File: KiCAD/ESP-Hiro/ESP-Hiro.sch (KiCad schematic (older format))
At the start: 17 parts, among them U1 TPS54331D

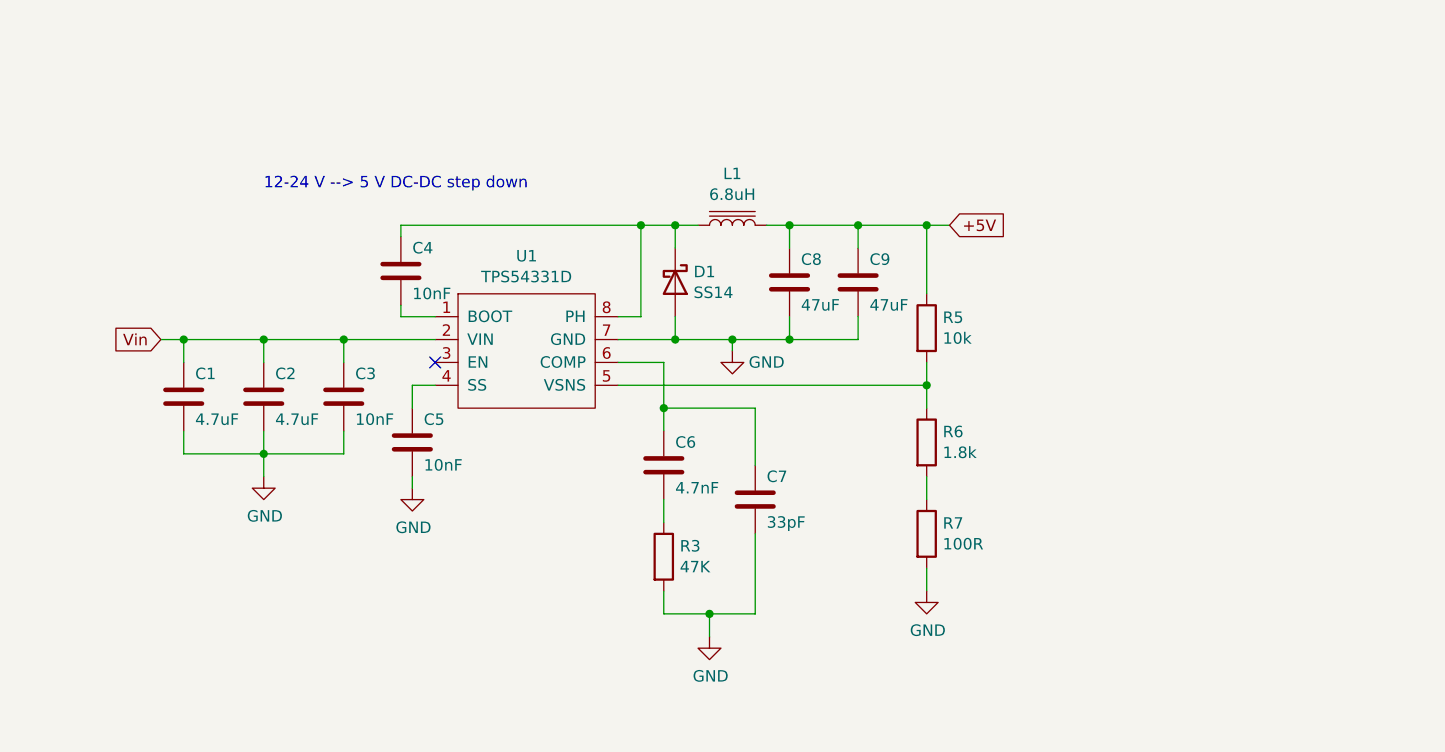
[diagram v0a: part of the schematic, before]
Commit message: Add 3.3 V LDO to schematic
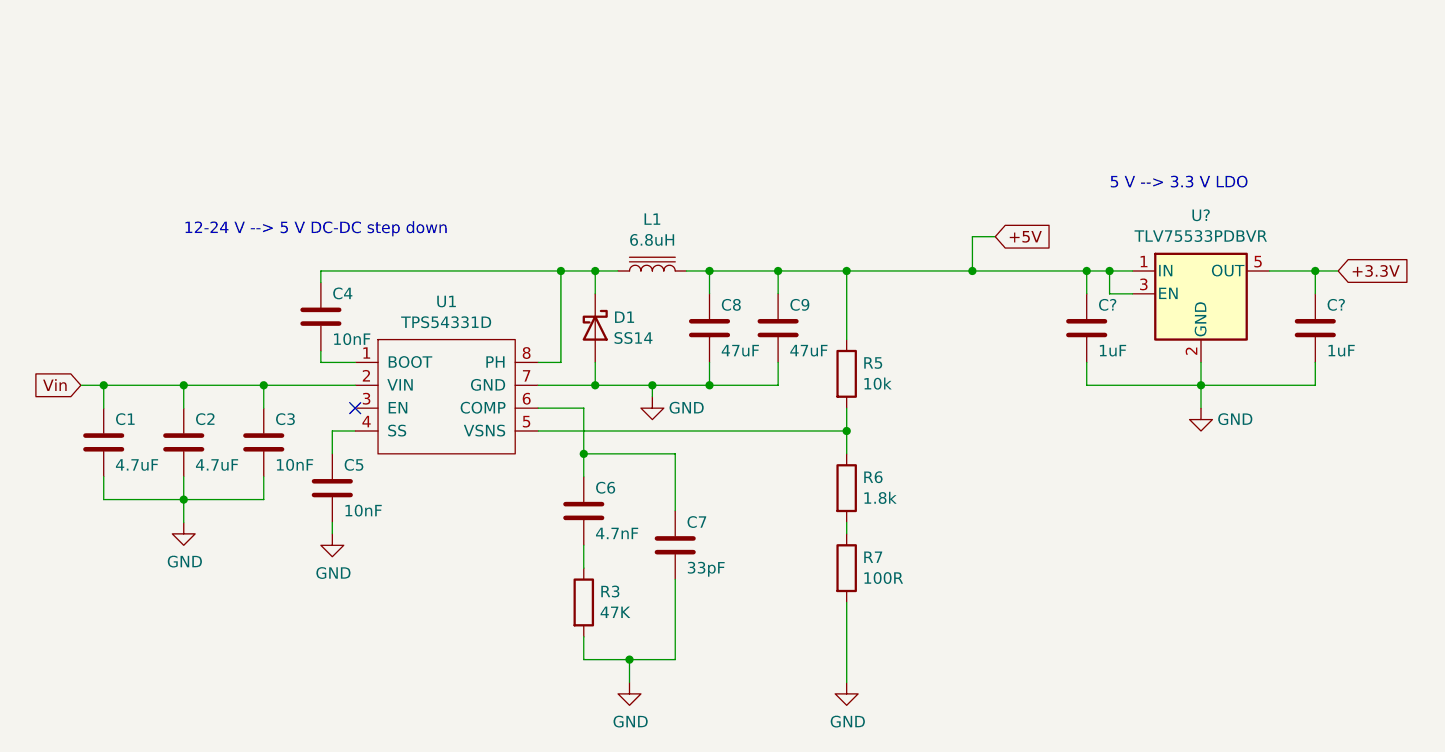
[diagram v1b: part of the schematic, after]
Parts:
- added C? (x2): 1uF, Capacitor_SMD:C_0603_1608Metric, symbol Device:C
- added U?: TLV75533PDBVR, Package_TO_SOT_SMD:SOT-23-5, symbol Regulator_Linear:TLV75533PDBV
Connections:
- net +5V: now also C?.1, U?.1 (IN), U?.3 (EN)
- net GND: now also C?.2, C?.2, U?.2 (GND)
- new net +3.3V: C?.1, U?.5 (OUT)
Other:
- note added: "5 V --> 3.3 V LDO"
- moved on the sheet: C1, C2, C3, C4, C5, C6, C7, C8, C9, D1, L1, R3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

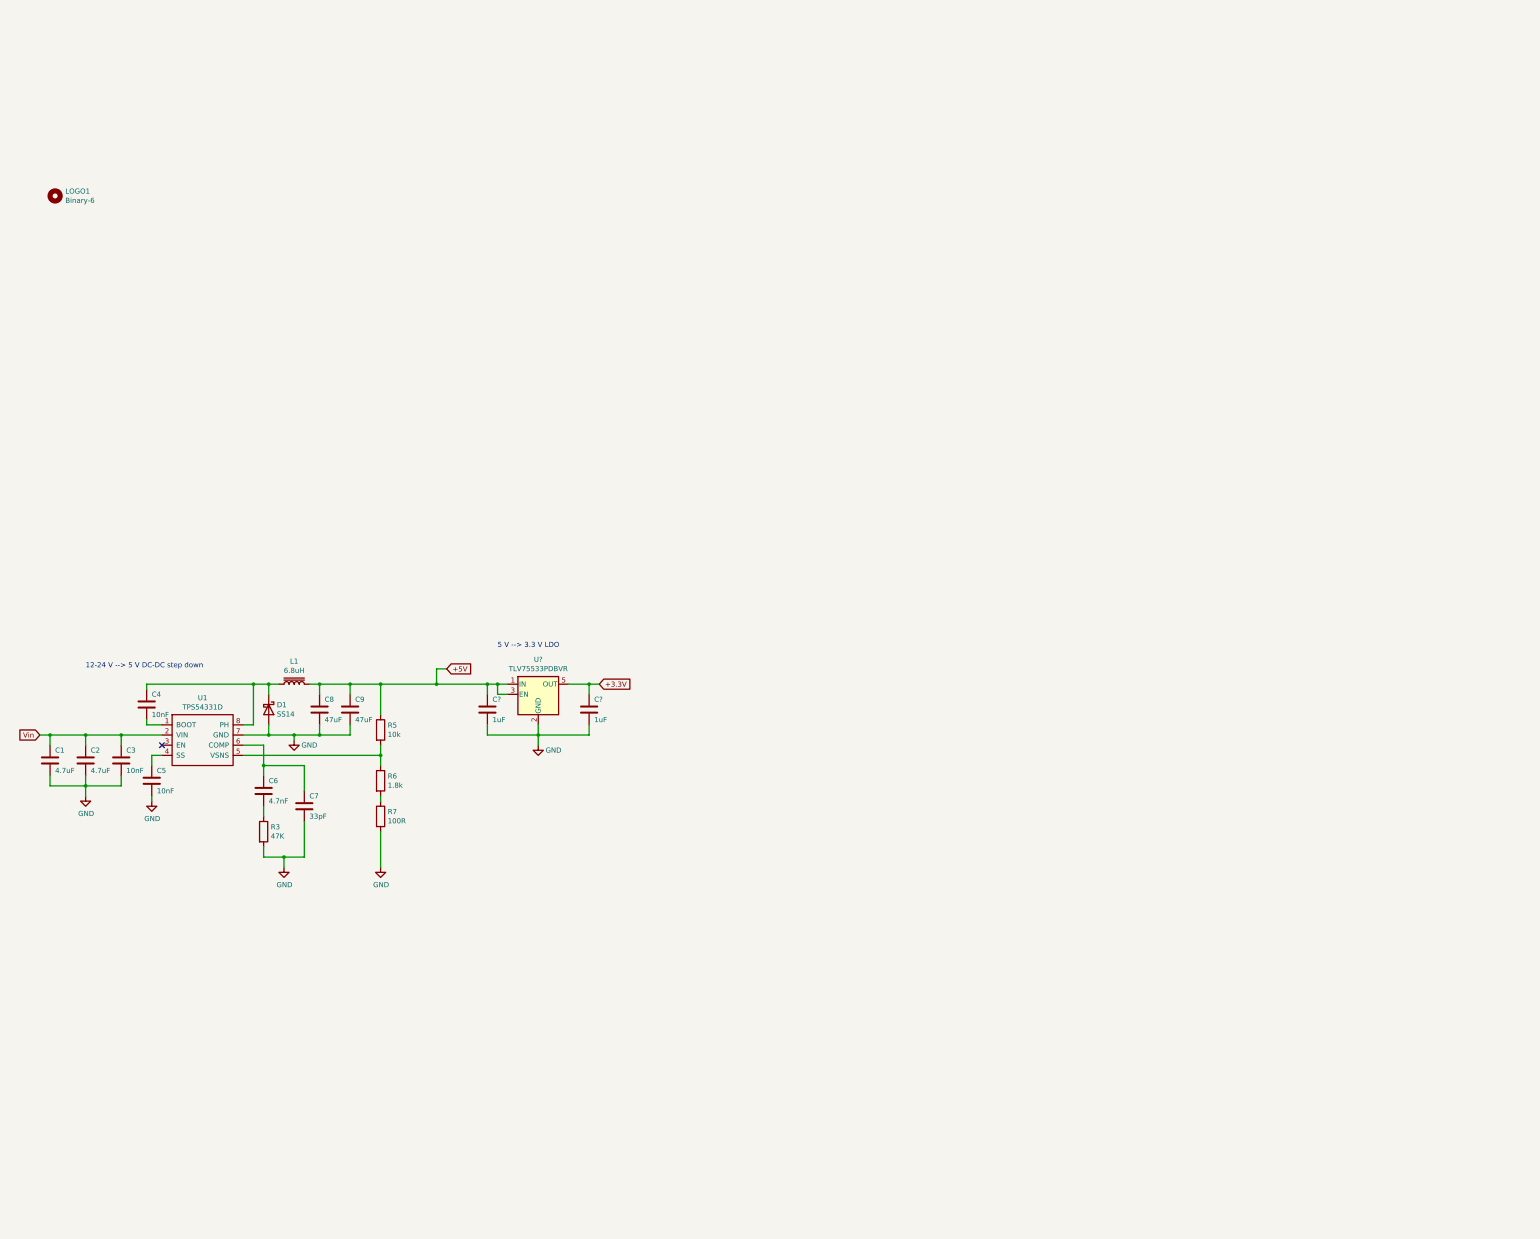
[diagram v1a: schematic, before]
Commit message: Paste more reusable blocks from old ESP-Hiro version into new schematic
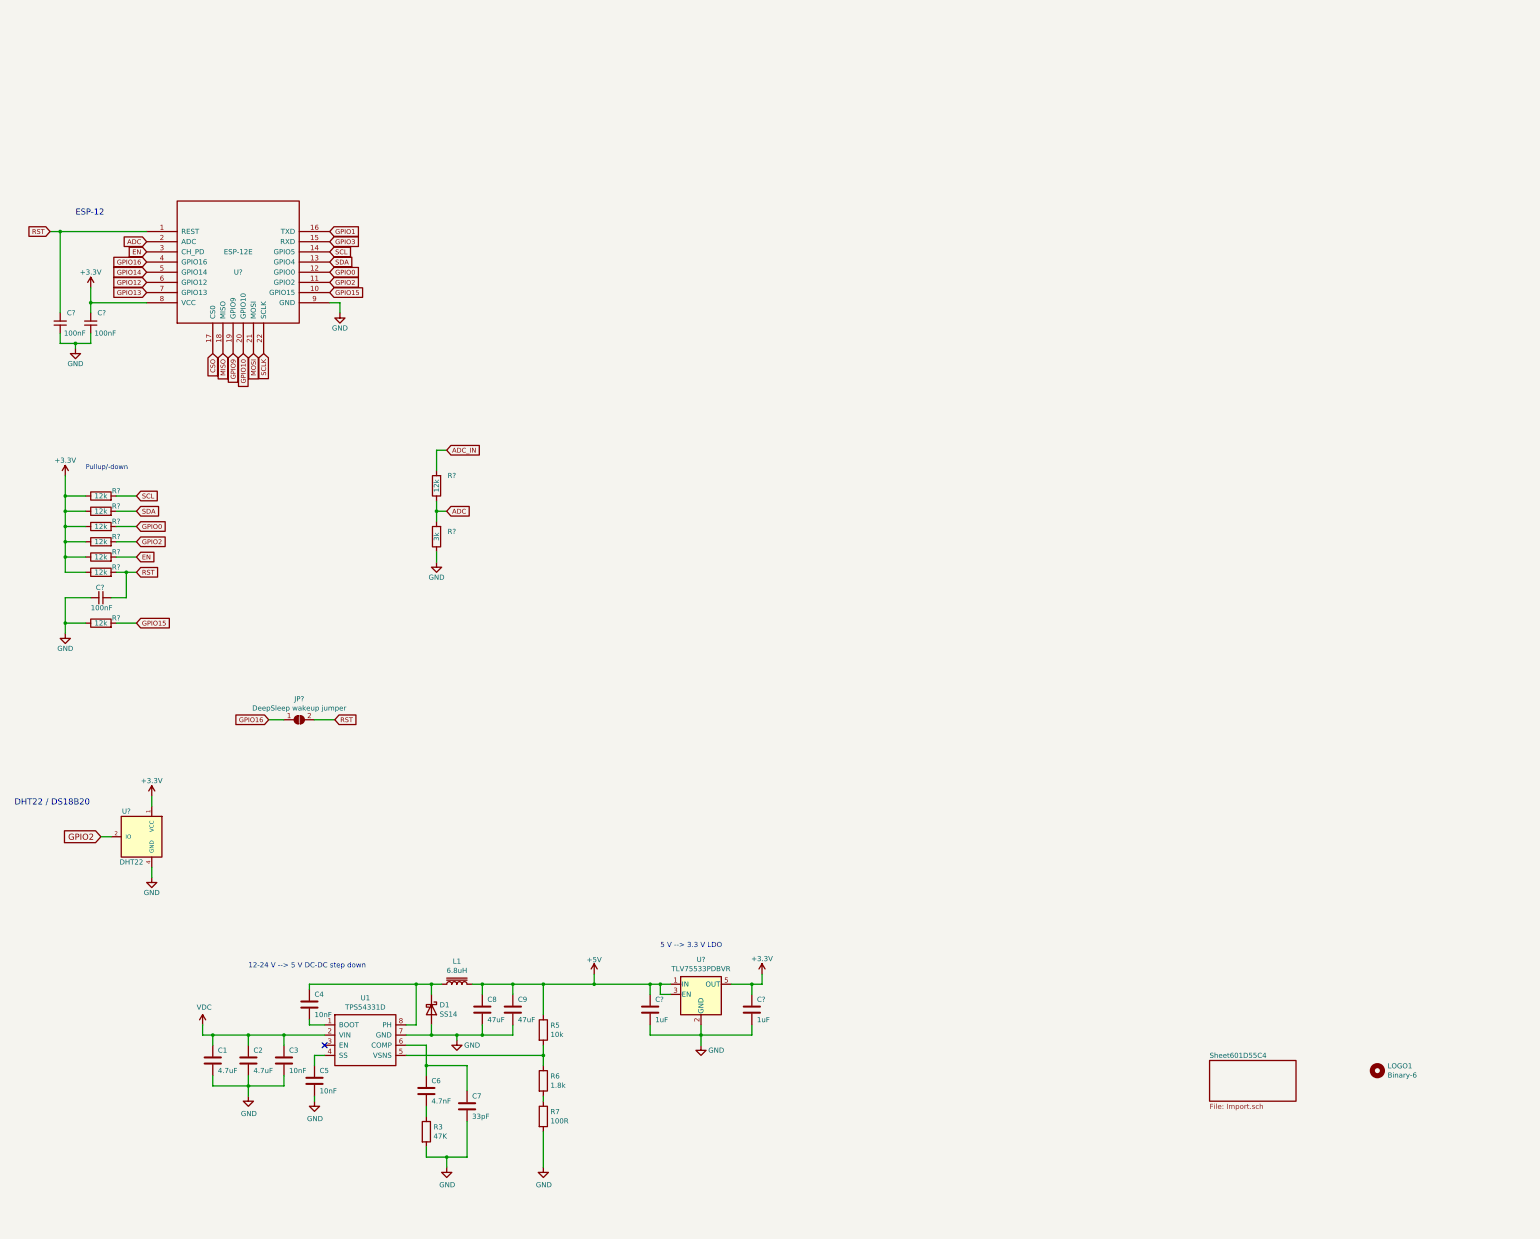
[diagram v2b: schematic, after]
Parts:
- added C? (x3): 100nF, Capacitor_SMD:C_0603_1608Metric, symbol Smart-Home-Erweiterung-rescue:C_Small-device-Smart-Home-Erweiterung-rescue
- added JP?: DeepSleep wakeup jumper, symbol Jumper:SolderJumper_2_Open
- added R?: 3k, Resistor_SMD:R_0603_1608Metric, symbol Smart-Home-Erweiterung-rescue:R-device-Smart-Home-Erweiterung-rescue
- added R? (x8): 12k, Resistor_SMD:R_0603_1608Metric, symbol Smart-Home-Erweiterung-rescue:R-device-Smart-Home-Erweiterung-rescue
- added U?: ESP-12E, ESP8266:ESP-12E_SMD, symbol Smart-Home-Erweiterung-rescue:ESP-12E-Smart-Home-Erweiterung-rescue
- added U?: DHT22, Sensors:DHT22_Temperature_Humidity, symbol Smart-Home-Erweiterung-rescue:DHT11-Smart-Home-Erweiterung-rescue
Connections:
- net GND: now also C?.1, C?.1, C?.2, R?.1, R?.1, U?.4 (GND), U?.9 (GND)
- net +3.3V renamed +3V3
- net +3V3: now also C?.2, R?.1, R?.1, R?.1, R?.1, R?.1, R?.1, U?.1 (VCC), U?.8 (VCC)
- net Vin renamed VDC
- new net ADC: R?.1, R?.2, U?.2 (ADC)
- new net ADC_IN: R?.2
- new net CSO: U?.17 (CS0)
- new net EN: R?.2, U?.3 (CH_PD)
- new net GPIO0: R?.2, U?.12 (GPIO0)
- new net GPIO1: U?.16 (TXD)
- new net GPIO10: U?.20 (GPIO10)
- new net GPIO12: U?.6 (GPIO12)
- new net GPIO13: U?.7 (GPIO13)
- new net GPIO14: U?.5 (GPIO14)
- new net GPIO15: R?.2, U?.10 (GPIO15)
- new net GPIO16: JP?.1 (A), U?.4 (GPIO16)
- new net GPIO2: R?.2, U?.11 (GPIO2), U?.2 (IO)
- new net GPIO3: U?.15 (RXD)
- new net GPIO9: U?.19 (GPIO9)
- new net MISO: U?.18 (MISO)
- new net MOSI: U?.21 (MOSI)
- new net RST: C?.1, C?.2, JP?.2 (B), R?.2, U?.1 (REST)
- new net SCL: R?.2, U?.14 (GPIO5)
- new net SCLK: U?.22 (SCLK)
- new net SDA: R?.2, U?.13 (GPIO4)
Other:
- note added: "DHT22 / DS18B20"
- note added: "ESP-12"
- note added: "Pullup/-down"
- moved on the sheet: C1, C2, C3, C4, C5, C6, C7, C8, C9, C?, D1, L1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

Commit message: dump parts onto PCB
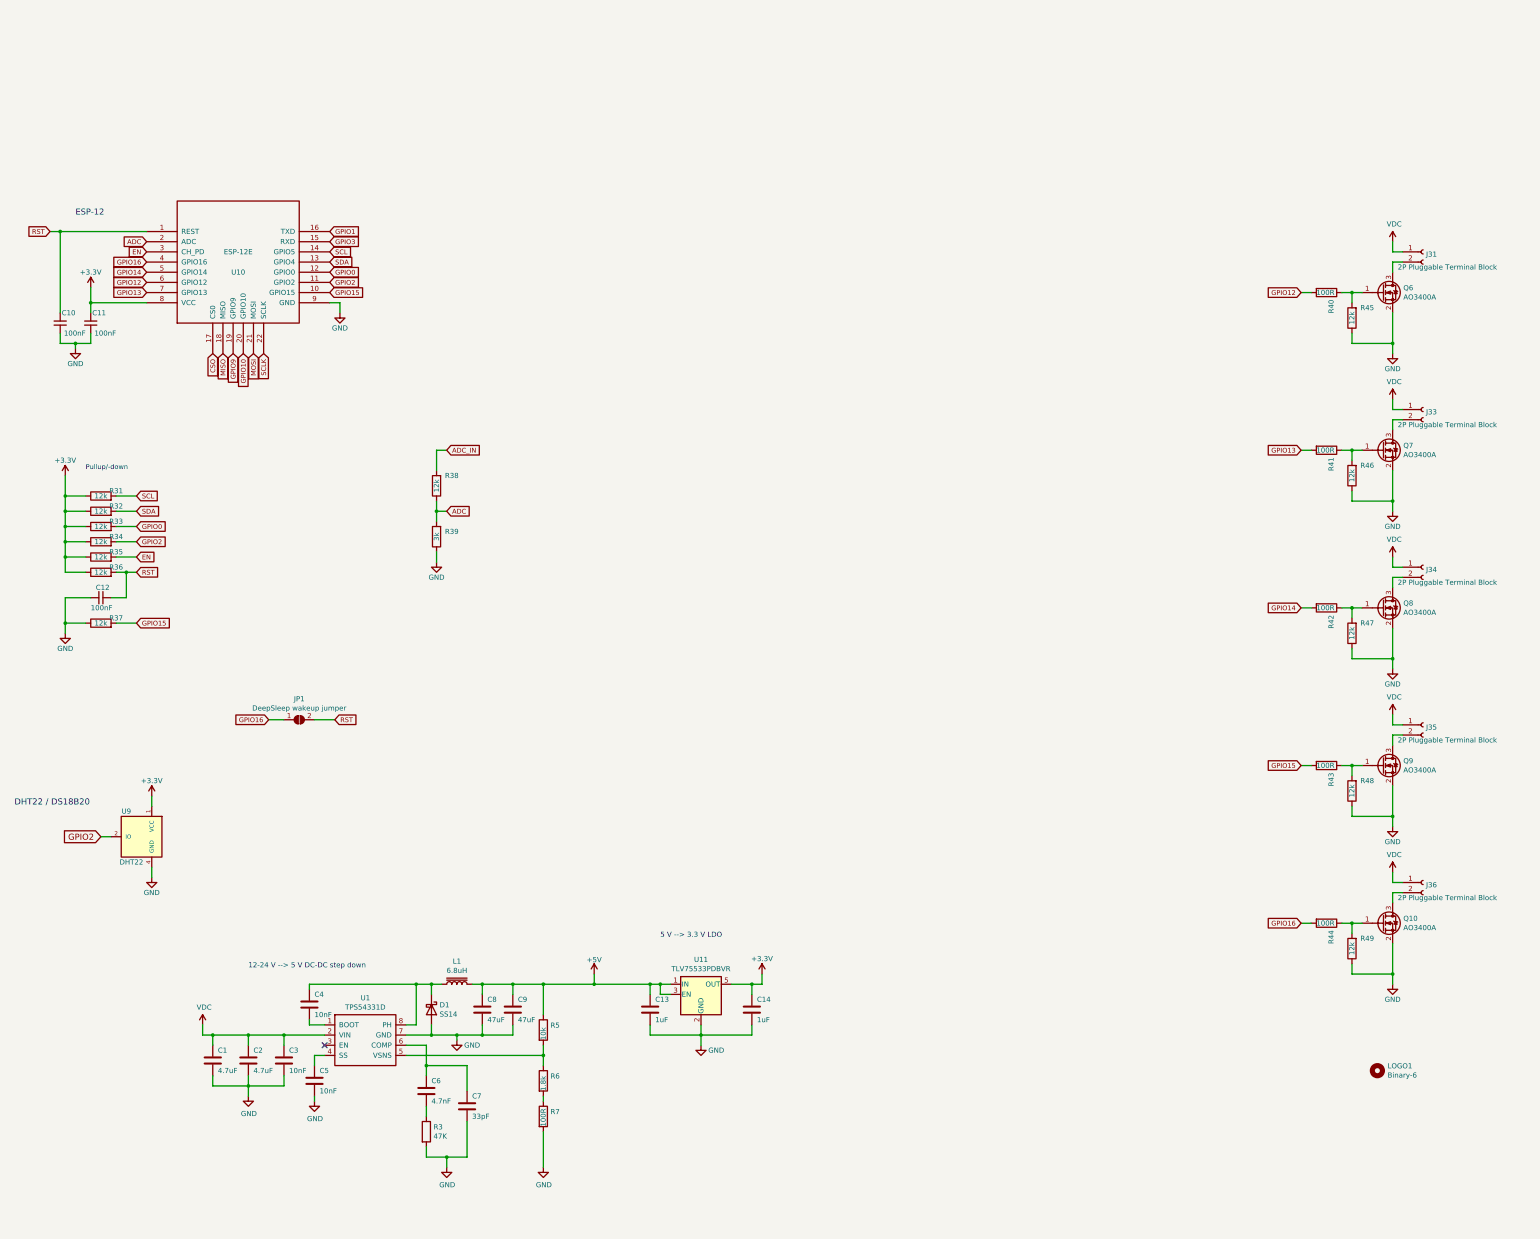
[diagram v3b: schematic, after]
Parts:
- added J31, J33, J34, J35, J36: 2P Pluggable Terminal Block, Connector_Phoenix_MSTB:PhoenixContact_MSTBA_2,5_2-G-5,08_1x02_P5.08mm_Horizontal, symbol Connector:Conn_01x02_Female
- added Q10, Q6, Q7, Q8, Q9: AO3400A, Package_TO_SOT_SMD:SOT-23, symbol Transistor_FET:AO3400A
- added R40, R41, R42, R43, R44: 100R, Resistor_SMD:R_0603_1608Metric, symbol Device:R
- added R45, R46, R47, R48, R49: 12k, Resistor_SMD:R_0603_1608Metric, symbol Smart-Home-Erweiterung-rescue:R-device-Smart-Home-Erweiterung-rescue
- JP1: renamed from JP?; footprint (none) -> Jumper:SolderJumper-2_P1.3mm_Open_TrianglePad1.0x1.5mm
- L1: footprint MeineBibpretty:Sunltech_SLO0630H -> MeineBib:Sunltech_SLO0630H
- LOGO1: footprint MeineBibpretty:Binary_6_v0.1 -> MeineBib:Binary_6_v0.1
- R6: LCSC C22843 -> C4177
- R7: LCSC C22828 -> C22775
- gave numbers to parts that had none: 17
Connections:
- net GND: now also Q10.2 (S), Q6.2 (S), Q7.2 (S), Q8.2 (S), Q9.2 (S), R45.1, R46.1, R47.1, R48.1, R49.1
- net GPIO12: now also R40.2
- net GPIO13: now also R41.2
- net GPIO14: now also R42.2
- net GPIO15: now also R43.2
- net GPIO16: now also R44.2
- net VDC: now also J31.1 (Pin_1), J33.1 (Pin_1), J34.1 (Pin_1), J35.1 (Pin_1), J36.1 (Pin_1)
- new net: Q7.1 (G), R41.1, R46.2
- new net: J33.2 (Pin_2), Q7.3 (D)
- new net: Q6.1 (G), R40.1, R45.2
- new net: J31.2 (Pin_2), Q6.3 (D)
- new net: Q8.1 (G), R42.1, R47.2
- new net: J34.2 (Pin_2), Q8.3 (D)
- new net: Q9.1 (G), R43.1, R48.2
- new net: J35.2 (Pin_2), Q9.3 (D)
- new net: Q10.1 (G), R44.1, R49.2
- new net: J36.2 (Pin_2), Q10.3 (D)

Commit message: General work on schematic
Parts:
- added J6: Conn_ADC, symbol Connector:Conn_01x02_Female
- J1: renamed from J31; value 2P Pluggable Terminal Block -> Conn_Q1
- J2: renamed from J33; value 2P Pluggable Terminal Block -> Conn_Q2
- J3: renamed from J34; value 2P Pluggable Terminal Block -> Conn_Q3
- J4: renamed from J35; value 2P Pluggable Terminal Block -> Conn_Q4
- J5: renamed from J36; value 2P Pluggable Terminal Block -> Conn_Q5
- U1: renamed from U9; value DHT22 -> DHT22/DS18B20 header
- renumbered C10 to C1, C7 to C10, C8 to C11, C9 to C12, C11 to C2, C12 to C3, C1 to C4, C2 to C5, C3 to C6, C4 to C7, C5 to C8, C6 to C9, Q6 to Q1, Q7 to Q2, Q8 to Q3, Q9 to Q4, Q10 to Q5, R31 to R1, R39 to R10, R5 to R11, R6 to R12, R7 to R13, R40 to R14, R41 to R15, R42 to R16, R43 to R17, R44 to R18, R45 to R19, R32 to R2, R46 to R20, R47 to R21, R48 to R22, R49 to R23, R33 to R3, R34 to R4, R35 to R5, R36 to R6, R37 to R7, R3 to R8, R38 to R9, U10 to U2, U1 to U3, U11 to U4
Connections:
- net GND: now also J6.1 (Pin_1)
- net ADC_IN: no longer names the net of R9.2
- net ADC_IN: now also J6.2 (Pin_2)
- net CSO: no longer names the net of U2.17 (CS0)
- net GPIO10: no longer names the net of U2.20 (GPIO10)
- net GPIO9: no longer names the net of U2.19 (GPIO9)
- net MISO: no longer names the net of U2.18 (MISO)
- net MOSI: no longer names the net of U2.21 (MOSI)
- net SCLK: no longer names the net of U2.22 (SCLK)
- no-connect marks 1 -> 7
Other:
- note added: "ADC"
- note removed: "DHT22 / DS18B20"
